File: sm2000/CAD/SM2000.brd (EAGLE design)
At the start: 160 x 100 mm, 353 parts, among them CN1 HDR100-3, CN10 ST-3509, CN11 HDR100-3, CN2 JS-MU3-002, CN3 DS-0518, CN5 ST-3509, CN8 ST-3509, J1 JMP-2PIN, J2 JMP-2PIN, J3 JMP-2PIN, J4 CONN-BOOM-XH-2A, P10 TPAD50, P11 TPAD50, P12 TPAD50, P13 TPAD50, P14 TPAD50, P16 TPAD50, P18 TPAD50, P19 TPAD50, P20 TPAD50, P21 TPAD50, P3 TPAD50, P4 TPAD50, P5 TPAD50, P6 TPAD50, P7 TPAD50, P8 TPAD50, P9 TPAD50, Q1 MMBT3904, Q12 BRF92, Q13 BFQ19, Q14 RD01MUS2, Q17 MMT2904, Q18 MMT2904, Q2 MMBT3904, Q3 MMBT3904, Q4 MMBT3904, Q5 MMBT3904, Q6 MMBT3904, Q7 BC548, Q8 BC549, SW1 SW-LC2259, SW2 TS-026, SW3 SW-LC2259EENP, SW4 TS-026, SW5 TS-02B, U1 STM32F405VGT6, U10 DNL, U11 L78MXX, U12 PGA-103+, U13 ADE-1, U14 SI570CAC000141DG, U15 SI5351A, U2 L78MXX, U3 STMPS2141, U4 EMIF02-USB03F2, U5 L78MXX, U6 LD3985M33R, U7 SA612A, U8 LM386M-1, U9 LMV341, X1 BU-SMA-H, X2 BU-SMA-H

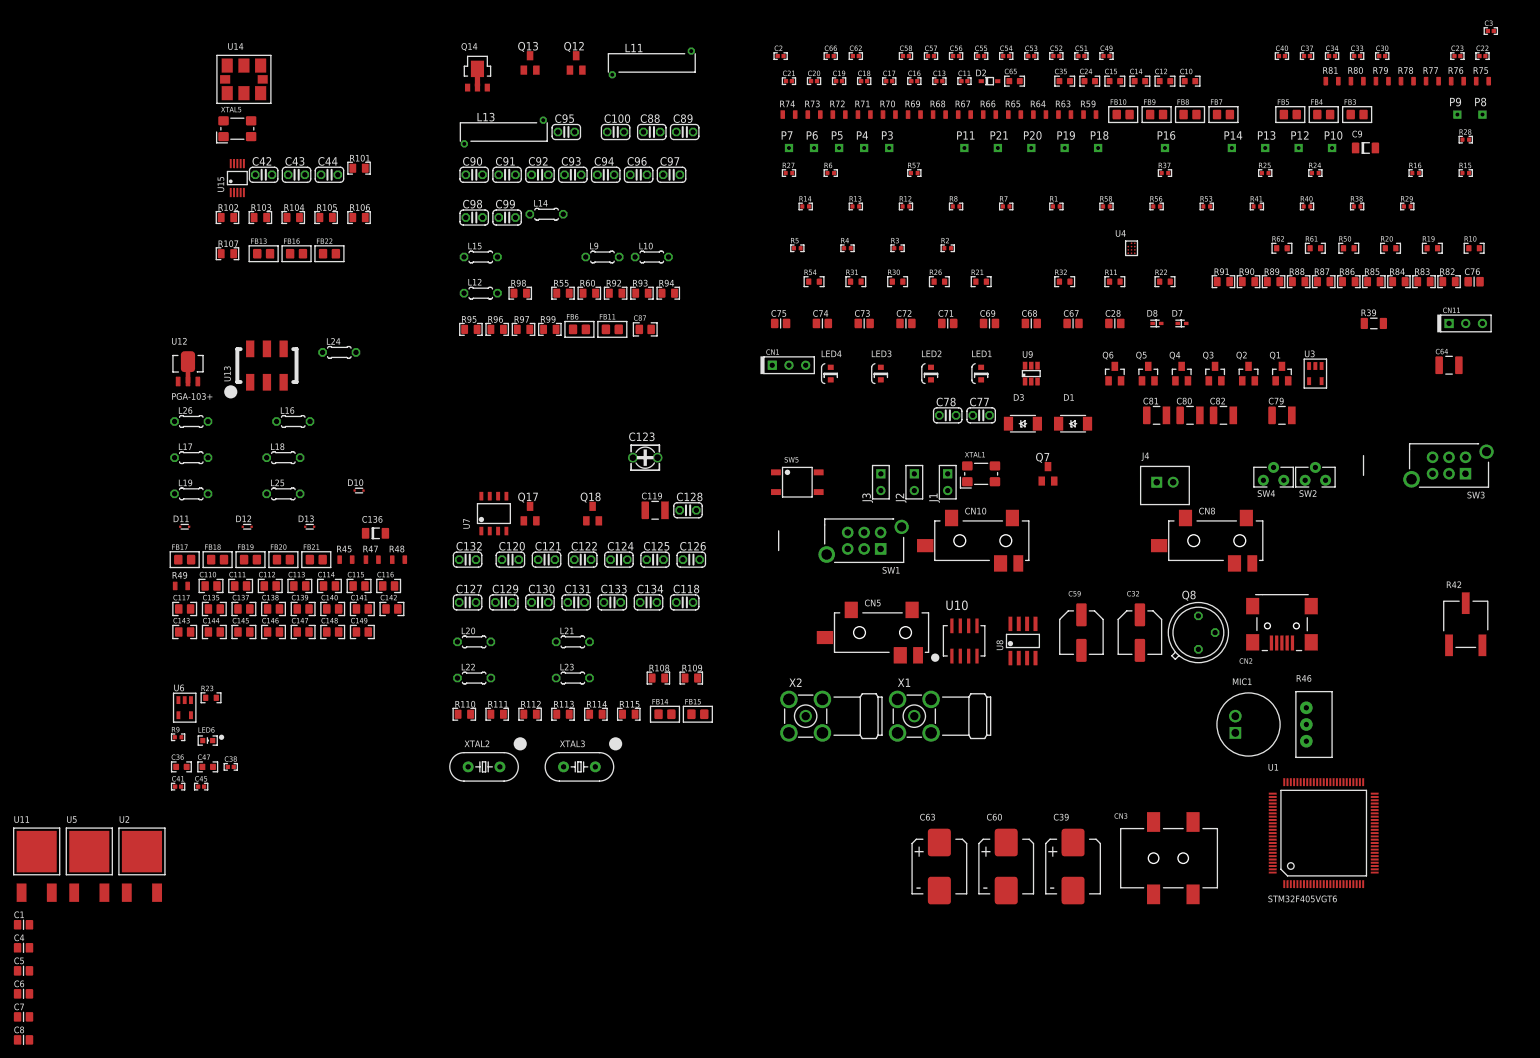
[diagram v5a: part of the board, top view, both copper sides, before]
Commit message: Added Circuitry for +12_TX and +12V_RX. Need to add +12V_TX_ENB and +12V_RX_ENB to CPU. Used P-Channel mosfet for voltage SW and MMBT3904 to control sw(price). See Pg 3.
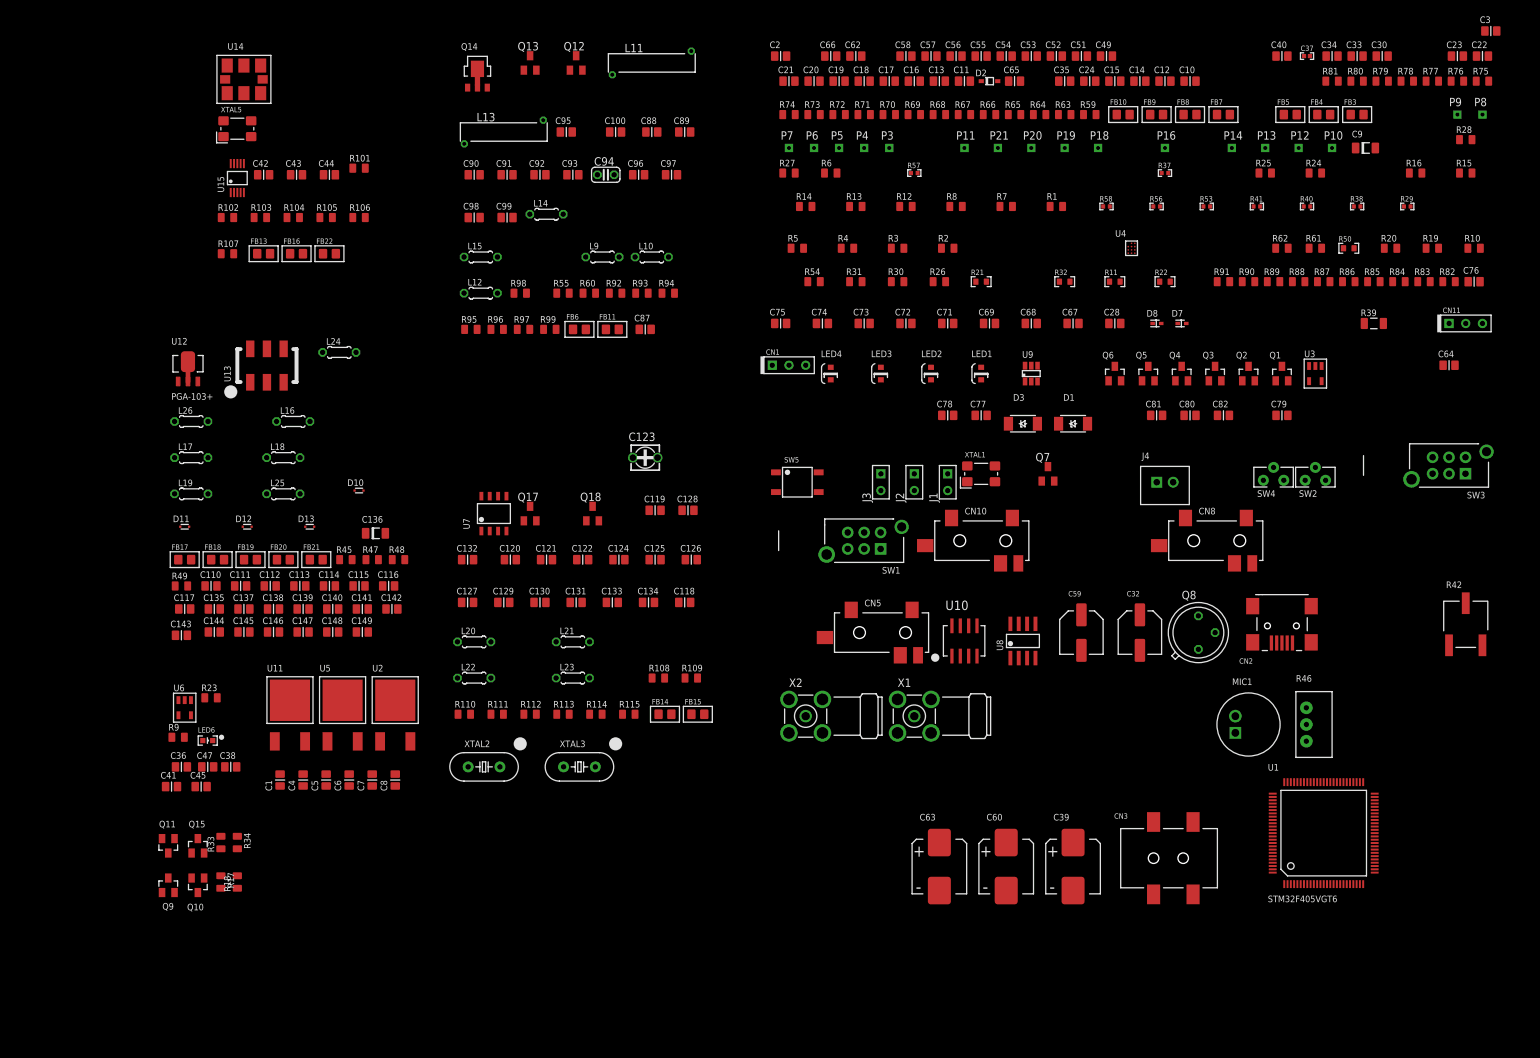
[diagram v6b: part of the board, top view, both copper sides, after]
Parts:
- added Q10, Q15: MMBT3904, _RoweTel:SOT23
- added Q11, Q9: STR2P3LLH6, _RoweTel:SOT23
- added R17, R33: 2.2K,1/8W,5%, _RoweTel:R0805
- added R18, R34: 10K,1/8W,5%, _RoweTel:R0805
- C1, C5, C7: value .33uF,25V,CER -> .33uF,25V
- C10, C12, C14, C15, C24, C35, C36, C47, C65: device AA-ipc-7351-capacitor:CAPC1608X92N -> _RoweTel:C0805
- C100, C118, C120, C121, C122, C124, C125, C126, C127, C128, C129, C130, C131, C132, C133, C134, C42, C43, C44, C77, C78, C88, C89, C90, C91, C92, C93, C95, C96, C97, C98, C99: device rcl:C025-024X044 -> _RoweTel:C0805
- C11, C13, C16, C17, C18, C19, C2, C20, C21, C22, C23, C3, C30, C33, C34, C38, C40, C41, C45, C49, C51, C52, C53, C54, C58, C62, C66: device AA-ipc-7351-capacitor:CAPC1005X60N -> _RoweTel:C0805
- C110, C111, C112, C113, C114, C115, C116, C117, C135, C137, C138, C139, C140, C141, C142, C143, C144, C145, C146, C147, C148, C149, C87: device AA-ipc-7351-capacitor:CAPC2012X145AN -> _RoweTel:C0805
- C119, C79, C80, C81, C82: device _RoweTel:C1210 -> _RoweTel:C0805
- C4, C6: value 100nF,25V,CER -> 100nF,25V
- C55, C56: value 1nF,25V,0402 -> 1nF,25V; device AA-ipc-7351-capacitor:CAPC1005X60N -> _RoweTel:C0805
- C57: value 3.9nF,16V,0402 -> 3.9nF,16V; device AA-ipc-7351-capacitor:CAPC1005X60N -> _RoweTel:C0805
- C64: value 22uF,25V,1210 -> 22uF,25V; device AA-ipc-7351-capacitor:CAPC3225X168N -> _RoweTel:C0805
- C8: value 100nF,25V,cer -> 100nF,25V
- R1, R12, R13, R14, R15, R16, R2, R24, R25, R27, R28, R3, R4, R5, R6, R7, R8, R9: device AA-ipc-7351-resistor:RESC1005X40AN -> _RoweTel:R0805
- R10, R19, R20, R23, R26, R30, R31, R54, R61, R62: device AA-ipc-7351-resistor:RESC1608X55N -> _RoweTel:R0805
- R101, R102, R103, R104, R105, R106, R107, R108, R109, R110, R111, R112, R113, R114, R115, R55, R60, R82, R83, R84, R85, R86, R87, R88, R89, R90, R91, R92, R93, R94, R95, R96, R97, R98, R99: device AA-ipc-7351-resistor:RESC2012X70N -> _RoweTel:R0805
- R45, R47, R48, R49, R59, R63, R64, R65, R66, R67, R68, R69, R70, R71, R72, R73, R74, R75, R76, R77, R78, R79, R80, R81: device _RoweTel:RR0805 -> _RoweTel:R0805
- moved C8 68.9 mm to (-179.0, 2.50), turned to 90 degrees
- moved C7 64.1 mm to (-182.5, 2.50), turned to 90 degrees
- moved C6 59.2 mm to (-186.0, 2.50), turned to 90 degrees
- moved C5 54.4 mm to (-189.5, 2.50), turned to 90 degrees
- moved C4 49.6 mm to (-193.0, 2.50), turned to 90 degrees
- moved U11 44.8 mm to (-195.0, 11.5)
- moved U2 44.8 mm to (-179.0, 11.5)
- moved U5 44.8 mm to (-187.0, 11.5)
- moved C1 44.8 mm to (-196.5, 2.50), turned to 90 degrees
- moved C41 1.00 mm to (-213.0, 1.50)
- moved C143 0.71 mm to (-211.5, 24.5)
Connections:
- new net +12V_RX: Q11.3, Q9.3, R70.2
- new net +12V_RX_ENB: R18.1, R34.1
- new net N$30: C144.1
- new net N$36: C143.2
- new net N$38: C137.2
- new net N$40: R80.1
- new net N$42: Q10.3, Q9.1, R17.1
- new net N$50: Q11.1, Q15.3, R33.1
- new net N$53: Q10.1, R18.2
- new net N$55: Q15.1, R34.2
- net +12V: now also Q11.2, Q9.2, R17.2, R33.2; no longer R70.1, R80.1
- net GND: now also Q10.2, Q15.2
- net N$67: now also R70.1; no longer R70.2

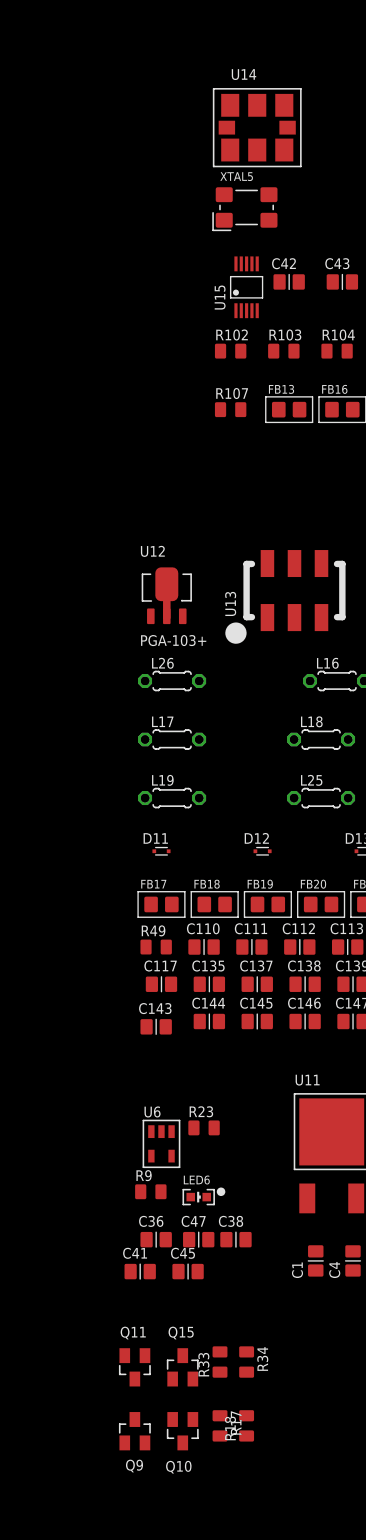
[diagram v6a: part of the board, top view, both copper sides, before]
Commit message: 
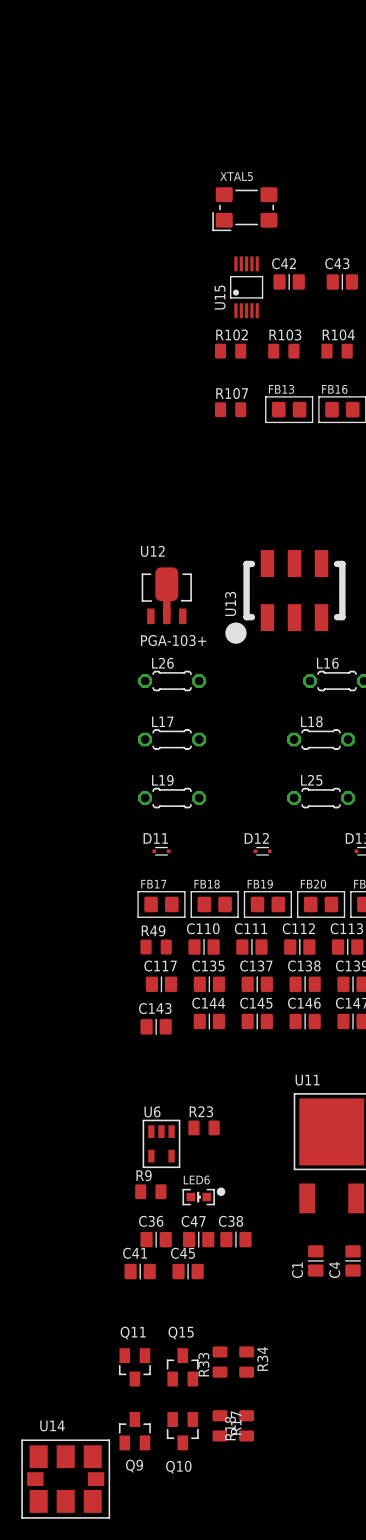
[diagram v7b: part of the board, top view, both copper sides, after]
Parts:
- C42, C43, C44: value 0.1u -> 0.1uF,25V
- C67, C68, C69, C71, C72, C73, C74, C75, C76: value 100nF -> 100nF,25V
- L20: value 5.7uH +/- 10% Q>20 -> 5.7uH
- L21: value 9.2uH +/- 10% Q>20 -> 9.2uH
- L22: value 5.2uH +/- 10% Q>20 -> 5.2uH
- L23: value 15uH +/- 10% Q>20 -> 15uH
- Q17, Q18: value MMT2904 -> MMBT3904
- U14: value SI570CAC000141DG -> SI570
- XTAL5: value 25MHz 10pF e.g. TXC 7B-25.000MEEQ-T -> 25MHz,TXC,SMD
- moved U14 128.3 mm to (-220.0, -18.0)
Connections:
- removed net 3V3: FB13.1, FB22.1
- removed net N$117: FB16.1
- new net N$56: L20.1
- new net SCL: U14.8, U15.4
- new net SDA: U14.7, U15.5
- net +12V_RX: no longer Q11.3
- net +3.3V: now also FB13.1, FB16.1, FB22.1
- net N$40: now also Q11.3

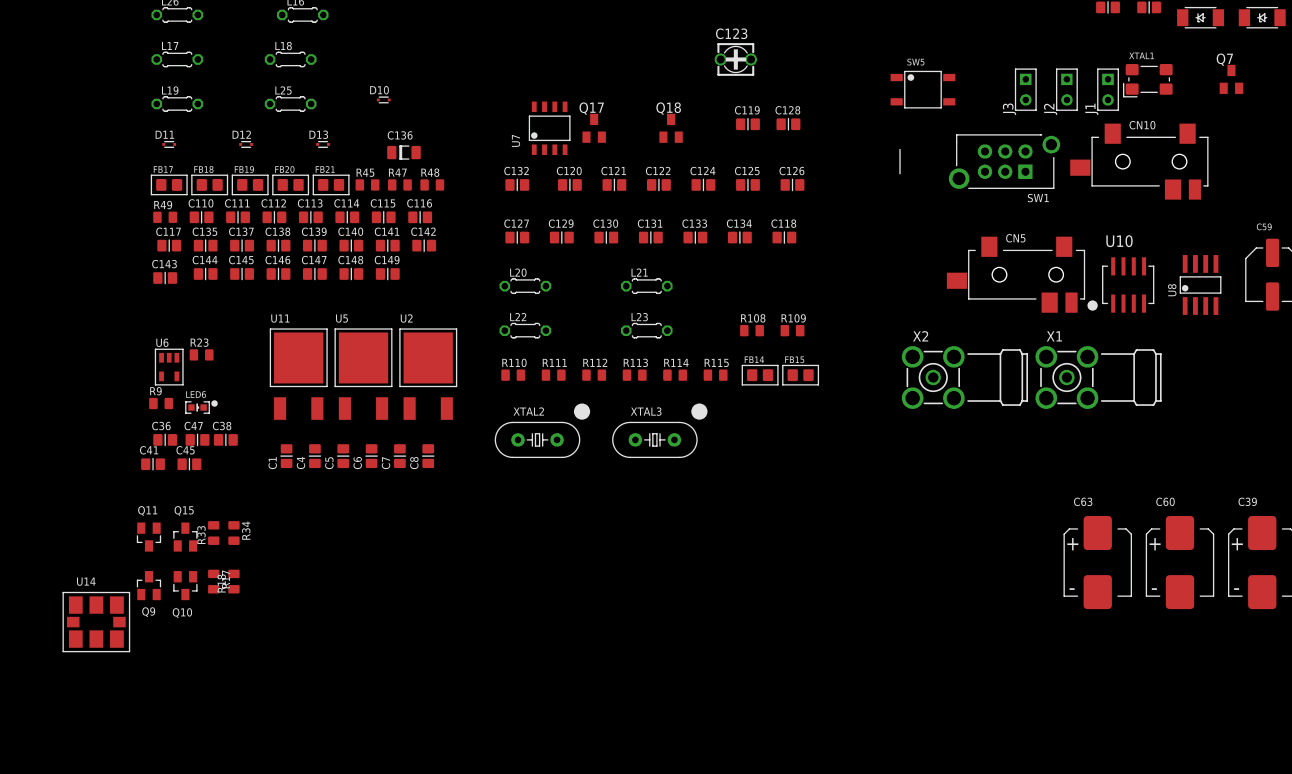
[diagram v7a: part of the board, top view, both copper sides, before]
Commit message: 
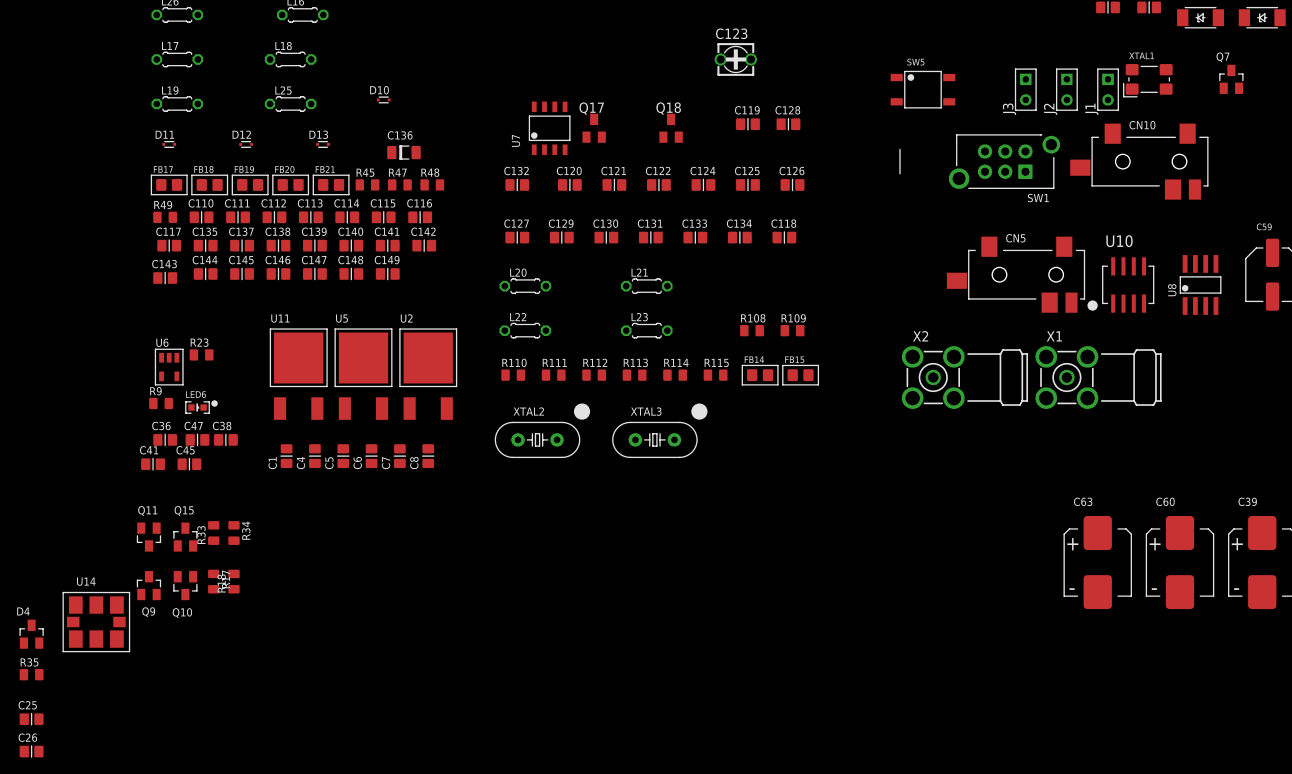
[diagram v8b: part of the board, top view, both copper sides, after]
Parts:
- added C25, C26: (no value), _RoweTel:C0805
- added D4: BAT18, _RoweTel:SOT23
- added R35: RES-0805, _RoweTel:R0805
- C77: value 0.1u -> 0.1uF,25V
- Q7: device transistor:SOT23-EBC -> _RoweTel:SOT23
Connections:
- new net AIN_PWR: C26.2, D4.1
- new net N$57: C25.1, D4.3, R35.2
- net ANT_SMA: now also C25.2
- net GND: now also C26.1, R35.1
- net N$101: now also Q7.2; no longer Q7.E
- net N$104: now also Q7.1; no longer Q7.B
- net N$105: now also Q7.3; no longer Q7.C
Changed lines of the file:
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@@
 <attribute name="OC_FARNELL" value="unknown" x="1.5" y="-17" size="1.778" layer="27" display="off"/>
 </element>
-<element name="Q7" library="transistor" package="SOT23-EBC" value="BC548" x="-79.78" y="49.04"/>
+<element name="Q7" library="_RoweTel" package="SOT23" value="BC548" x="-79.78" y="49.04"/>
 <element name="R82" library="_RoweTel" package="R0805" value="39k" x="-18.82" y="78.25"/>
 <element name="R83" library="_RoweTel" package="R0805" value="18k" x="-22.63" y="78.25"/>
@@
 <element name="R85" library="_RoweTel" package="R0805" value="3k3" x="-30.25" y="78.25"/>
 <element name="R86" library="_RoweTel" package="R0805" value="10" x="-34.06" y="78.25"/>
-<element name="C77" library="_RoweTel" package="C0805" value="0.1u" x="-89.94" y="57.93"/>
+<element name="C77" library="_RoweTel" package="C0805" value="0.1uF,25V" x="-89.94" y="57.93"/>
 <element name="C78" library="_RoweTel" package="C0805" value="0.1u" x="-95.02" y="57.93"/>
 <element name="R87" library="_RoweTel" package="R0805" value="10" x="-37.87" y="78.25"/>
@@
 </element>
 <element name="U14" library="_RoweTel" package="SI570" value="SI570" x="-220" y="-18"/>
+<element name="D4" library="_RoweTel" package="SOT23" value="BAT18" x="-228" y="-19.5"/>
+<element name="R35" library="_RoweTel" package="R0805" value="RES-0805" x="-228" y="-24.5"/>
+<element name="C25" library="_RoweTel" package="C0805" value="" x="-228" y="-30"/>
+<element name="C26" library="_RoweTel" package="C0805" value="" x="-228" y="-34"/>
 </elements>
 <signals>
@@
 <contactref element="U14" pad="3"/>
 <contactref element="U14" pad="3"/>
+<contactref element="C26" pad="1"/>
+<contactref element="R35" pad="1"/>
+<wire x1="-228.9" y1="-34" x2="-228.95" y2="-24.5" width="0" layer="19" extent="1-1"/>
+<wire x1="-217.46" y1="-20.1" x2="-228.95" y2="-24.5" width="0" layer="19" extent="1-1"/>
 <wire x1="-209.95" y1="-12.4" x2="-217.46" y2="-20.1" width="0" layer="19" extent="1-1"/>
 <wire x1="-208.05" y1="-8.6" x2="-209.95" y2="-12.4" width="0" layer="19" extent="1-1"/>
@@
 </signal>
 <signal name="N$101">
-<contactref element="Q7" pad="E"/>
+<contactref element="Q7" pad="2"/>
 <contactref element="R84" pad="2"/>
 <contactref element="C79" pad="1"/>
 <wire x1="-45.12" y1="57.93" x2="-25.49" y2="78.25" width="0" layer="19" extent="1-1"/>
-<wire x1="-80.73" y1="47.94" x2="-45.12" y2="57.93" width="0" layer="19" extent="1-1"/>
+<wire x1="-78.83" y1="47.94" x2="-45.12" y2="57.93" width="0" layer="19" extent="1-1"/>
 </signal>
 <signal name="N$102">
@@
 <signal name="N$104">
 <contactref element="R83" pad="2"/>
-<contactref element="Q7" pad="B"/>
+<contactref element="Q7" pad="1"/>
 <contactref element="R82" pad="1"/>
 <wire x1="-21.68" y1="78.25" x2="-19.77" y2="78.25" width="0" layer="19" extent="1-1"/>
-<wire x1="-78.83" y1="47.94" x2="-21.68" y2="78.25" width="0" layer="19" extent="1-1"/>
+<wire x1="-80.73" y1="47.94" x2="-21.68" y2="78.25" width="0" layer="19" extent="1-1"/>
 </signal>
 <signal name="N$105">
-<contactref element="Q7" pad="C"/>
+<contactref element="Q7" pad="3"/>
 <contactref element="R88" pad="1"/>
 <contactref element="Q8" pad="2"/>
@@
 <contactref element="C147" pad="1"/>
 <contactref element="R48" pad="2"/>
+<contactref element="C25" pad="2"/>
 <wire x1="-177.55" y1="36" x2="-193.9" y2="25" width="0" layer="19" extent="1-1"/>
 <wire x1="-153.46" y1="88.5" x2="-177.55" y2="36" width="0" layer="19" extent="1-1"/>
 <wire x1="-146.4" y1="101" x2="-153.46" y2="88.5" width="0" layer="19" extent="1-1"/>
+<wire x1="-227.1" y1="-30" x2="-193.9" y2="25" width="0" layer="19" extent="1-1"/>
 </signal>
 <signal name="N$32">
@@
 <wire x1="-202.5" y1="91.8" x2="-217.1475" y2="-18" width="0" layer="19" extent="1-1"/>
 </signal>
+<signal name="N$57">
+<contactref element="C25" pad="1"/>
+<contactref element="D4" pad="3"/>
+<contactref element="R35" pad="2"/>
+<wire x1="-228.9" y1="-30" x2="-227.05" y2="-24.5" width="0" layer="19" extent="1-1"/>
+<wire x1="-228" y1="-18.4" x2="-227.05" y2="-24.5" width="0" layer="19" extent="1-1"/>
+</signal>
+<signal name="AIN_PWR">
+<contactref element="D4" pad="1"/>
+<contactref element="C26" pad="2"/>
+<wire x1="-227.1" y1="-34" x2="-228.95" y2="-20.6" width="0" layer="19" extent="1-1"/>
+</signal>
 </signals>
